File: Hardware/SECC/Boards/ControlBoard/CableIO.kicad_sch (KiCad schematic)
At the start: 8 parts

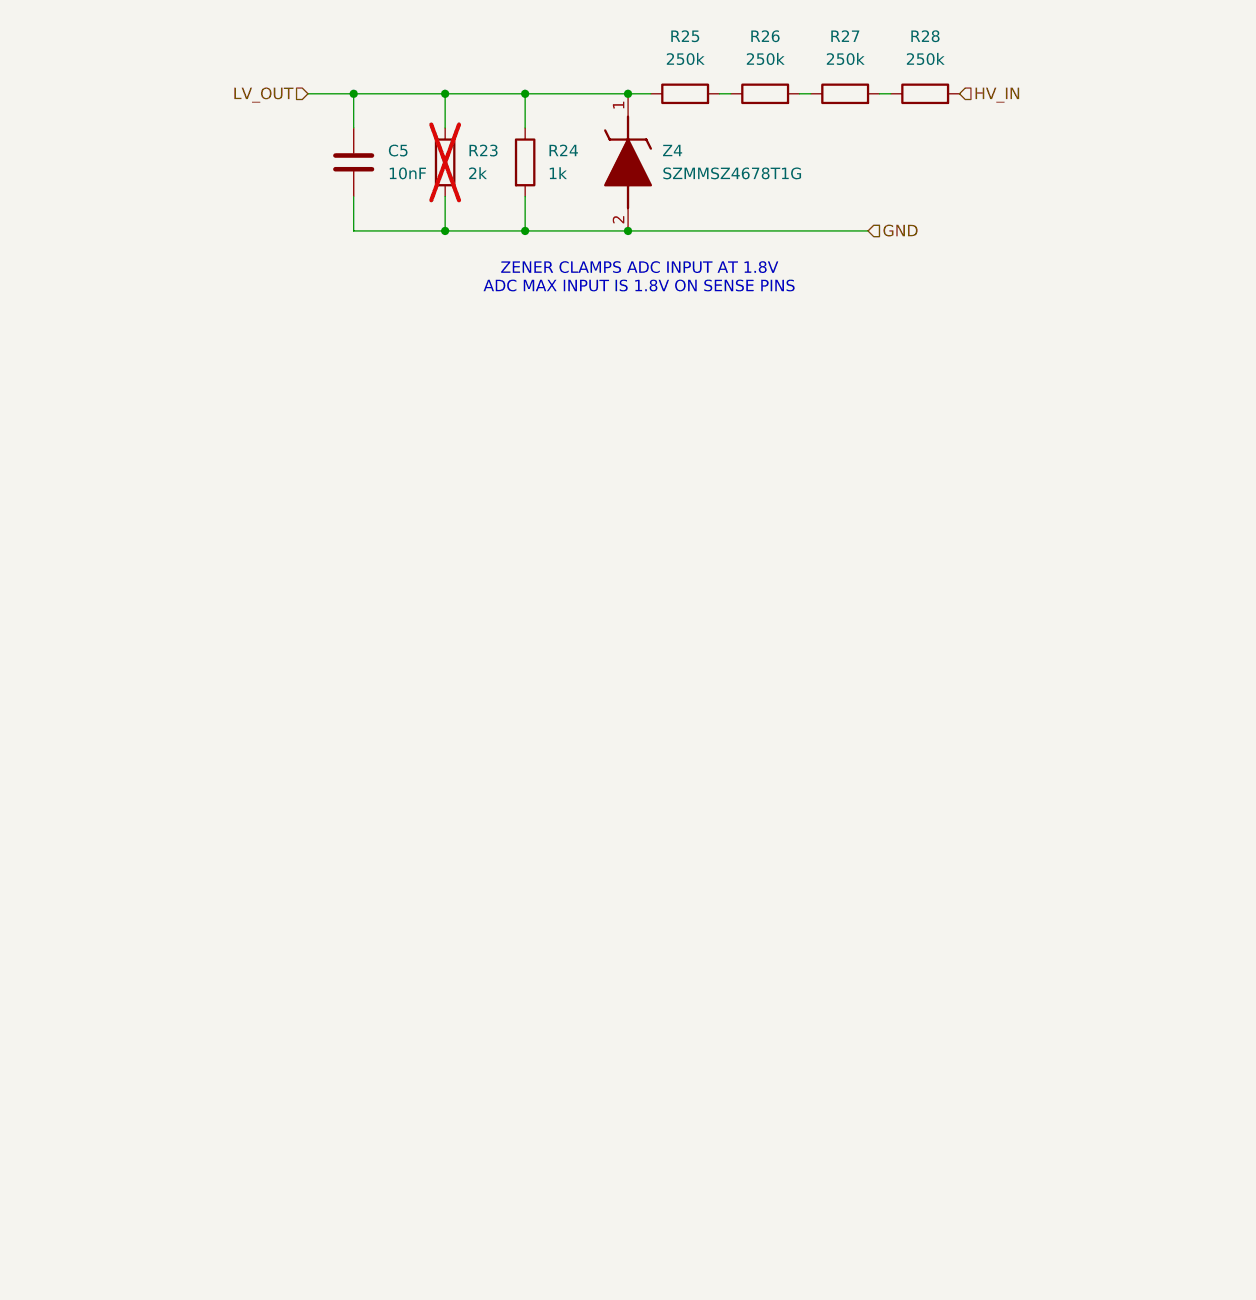
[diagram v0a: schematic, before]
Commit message: Update SECC Schematic
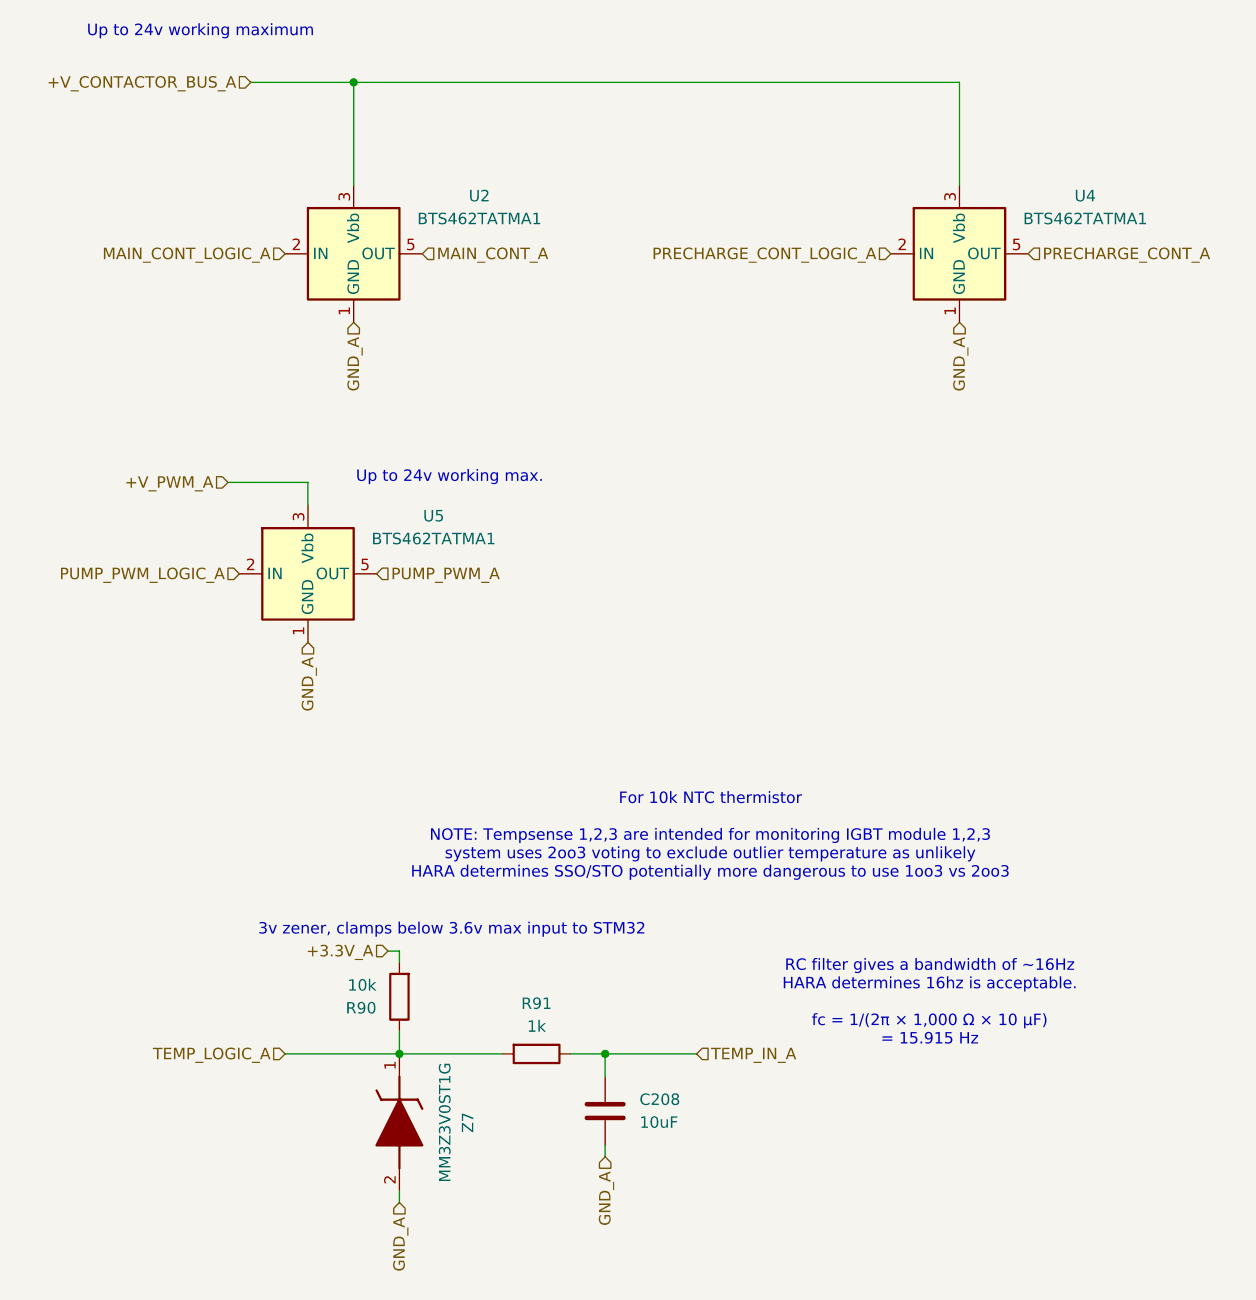
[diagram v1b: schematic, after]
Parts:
- removed C5: 10nF, Capacitor_SMD:C_1210_3225Metric_Pad1.33x2.70mm_HandSolder, symbol Device:C
- removed R23: 2k, Resistor_SMD:R_1210_3225Metric_Pad1.30x2.65mm_HandSolder, symbol Device:R
- removed R24: 1k, Resistor_SMD:R_1210_3225Metric_Pad1.30x2.65mm_HandSolder, symbol Device:R
- removed R25, R26, R27, R28: 250k, Resistor_SMD:R_1210_3225Metric_Pad1.30x2.65mm_HandSolder, symbol Device:R
- removed Z4: SZMMSZ4678T1G, InverterCom:SOD3716X135N, symbol InverterCom:SZMMSZ4678T1G
- added C208: 10uF, Capacitor_SMD:C_1210_3225Metric_Pad1.33x2.70mm_HandSolder, symbol Device:C
- added R90: 10k, Resistor_SMD:R_1210_3225Metric_Pad1.30x2.65mm_HandSolder, symbol Device:R
- added R91: 1k, Resistor_SMD:R_1210_3225Metric_Pad1.30x2.65mm_HandSolder, symbol Device:R
- added U2, U4, U5: BTS462TATMA1, Package_TO_SOT_SMD:TO-252-4, symbol Power_Management:BTS462TATMA1
- added Z7: MM3Z3V0ST1G, InverterCom:SOD2512X100N, symbol InverterCom:MM3Z3V0ST1G
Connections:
- new net +3.3V_A: R90.2
- new net +V_CONTACTOR_BUS_A: U2.3 (Vbb), U4.3 (Vbb)
- new net +V_PWM_A: U5.3 (Vbb)
- new net GND_A: C208.2, U2.1 (GND), U4.1 (GND), U5.1 (GND), Z7.2 (A)
- new net MAIN_CONT_A: U2.5 (OUT)
- new net MAIN_CONT_LOGIC_A: U2.2 (IN)
- new net PRECHARGE_CONT_A: U4.5 (OUT)
- new net PRECHARGE_CONT_LOGIC_A: U4.2 (IN)
- new net PUMP_PWM_A: U5.5 (OUT)
- new net PUMP_PWM_LOGIC_A: U5.2 (IN)
- new net TEMP_IN_A: C208.1, R91.1
- new net TEMP_LOGIC_A: R90.1, R91.2, Z7.1 (K)
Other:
- note added: "3v zener, clamps below 3.6v max input to STM32"
- note added: "For 10k NTC thermistor NOTE: Tempsense 1,2,3 are intended for monitoring IGBT module 1,2,3 system uses 2oo3 voting to exclude outlier temperature as unlikely HARA determines SSO/STO potentially more dangerous to use 1oo3 vs 2oo3"
- note added: "RC filter gives a bandwidth of ~16Hz HARA determines 16hz is acceptable. fc = 1/(2π × 1,000 Ω × 10 μF) = 15.915 Hz"
- note added: "Up to 24v working max."
- note added: "Up to 24v working maximum"
- note removed: "ZENER CLAMPS ADC INPUT AT 1.8V ADC MAX INPUT IS 1.8V ON SENSE PINS"

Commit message: Vendor BTS462TATMA1 symbol into InverterCom library
The symbol was referenced as Power_Management:BTS462TATMA1, which is
not vendored (project sym-lib-table only registers InverterCom) so
resolution silently depended on the machine's global KiCad symbol
libs. Copied the BTS462TATMA1 symbol verbatim from the installed
KiCad 10.0.3 stock library (self-contained, no extends; footprint
property stays Package_TO_SOT_SMD:TO-252-4, a stock global footprint)
into PartsLib/InverterCom.kicad_sym and repointed all lib_ids and
embedded lib_symbols copies (Chassis2 Power.kicad_sch, PowerSwitch
.kicad_sch, IOBoard.kicad_sch; SECC CableIO.kicad_sch) to
InverterCom:BTS462TATMA1. Vendored copy is byte-identical in content
to the embedded cached copies.
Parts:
- U2, U4, U5: symbol Power_Management:BTS462TATMA1 -> InverterCom:BTS462TATMA1
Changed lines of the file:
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@@
 	)
 	(symbol
-		(lib_id "Power_Management:BTS462TATMA1")
+		(lib_id "InverterCom:BTS462TATMA1")
 		(at 46.99 76.2 0)
 		(unit 1)
@@
 	)
 	(symbol
-		(lib_id "Power_Management:BTS462TATMA1")
+		(lib_id "InverterCom:BTS462TATMA1")
 		(at 119.38 40.64 0)
 		(unit 1)
@@
 	)
 	(symbol
-		(lib_id "Power_Management:BTS462TATMA1")
+		(lib_id "InverterCom:BTS462TATMA1")
 		(at 52.07 40.64 0)
 		(unit 1)
